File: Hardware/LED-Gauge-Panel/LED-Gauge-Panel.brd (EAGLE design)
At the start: 20.3 x 42.9 mm, 3 parts

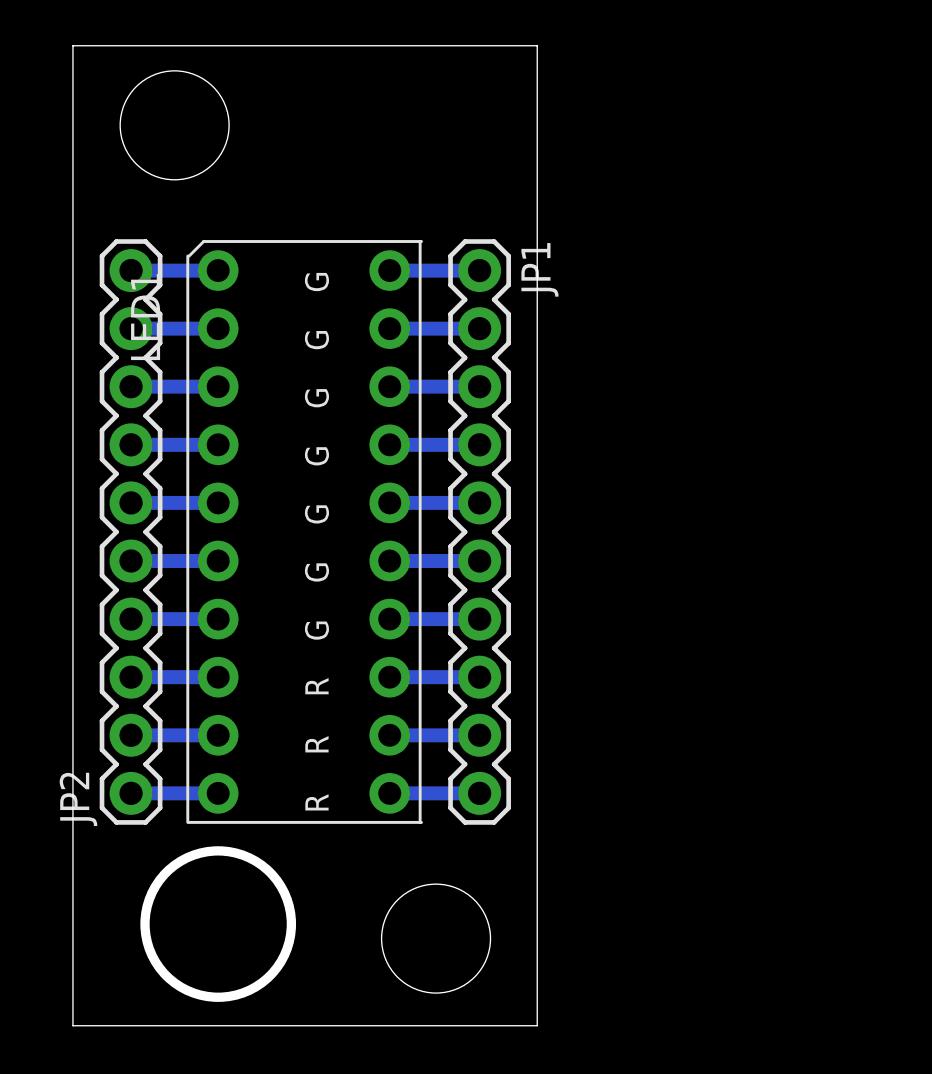
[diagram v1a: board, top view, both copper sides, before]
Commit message: Create library part for LED display button, update PCB with LED button part
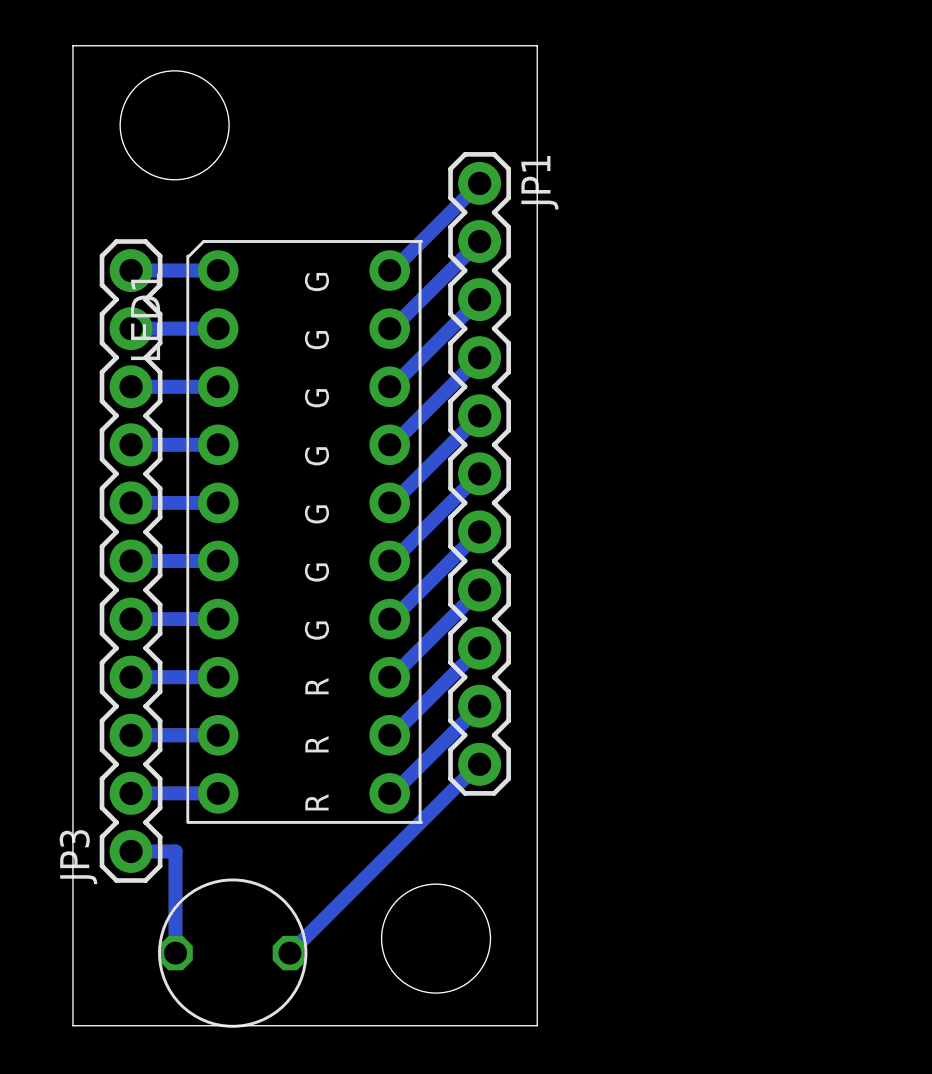
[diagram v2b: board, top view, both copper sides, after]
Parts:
- removed JP2: (no value), SparkFun-Connectors:1X10
- added JP3: (no value), SparkFun-Connectors:1X11
- added U$1: MOMENTARY-SWITCH-EVQ1, 2016PowerPackLibraries:EVQ11
- JP1: device SparkFun-Connectors:1X10 -> SparkFun-Connectors:1X11
- moved JP1 3.81 mm to (17.8, 36.8)
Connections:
- new net N$21: JP1.11, U$1.P$1
- new net N$22: JP3.1, U$1.P$2
- net N$11: now also JP3.11; no longer JP2.10
- net N$12: now also JP3.10; no longer JP2.9
- net N$13: now also JP3.9; no longer JP2.8
- net N$14: now also JP3.8; no longer JP2.7
- net N$15: now also JP3.7; no longer JP2.6
- net N$16: now also JP3.6; no longer JP2.5
- net N$17: now also JP3.5; no longer JP2.4
- net N$18: now also JP3.4; no longer JP2.3
- net N$19: now also JP3.3; no longer JP2.2
- net N$20: now also JP3.2; no longer JP2.1
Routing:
- net N$21: track 0.00 -> 11.7 mm
- net N$22: track 0.00 -> 6.39 mm
- net N$9: track 3.93 -> 5.51 mm
- net N$8: track 3.93 -> 5.51 mm
- net N$5: track 3.93 -> 5.51 mm
- net N$4: track 3.93 -> 5.51 mm
- net N$10: track 3.93 -> 5.51 mm
- net N$7: track 3.93 -> 5.51 mm
- net N$6: track 3.93 -> 5.51 mm
- net N$3: track 3.93 -> 5.51 mm
- net N$2: track 3.93 -> 5.51 mm
- net N$1: track 3.93 -> 5.51 mm
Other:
- outline, holes or cut-outs redrawn
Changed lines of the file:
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@@
 <hole x="15.875" y="3.81" drill="4.7625"/>
 <hole x="4.445" y="39.37" drill="4.7625"/>
-<circle x="6.35" y="4.445" radius="3.2" width="0.4064" layer="20"/>
 </plain>
 <attributes>
@@
 </autorouter>
 <elements>
-<element name="JP1" library="SparkFun-Connectors" package="1X10" value="" x="17.78" y="33.02" rot="R270">
-<attribute name="PROD_ID" value="CONN-11563" x="1.27" y="-5.08" size="1.778" layer="27" rot="R270" display="off"/>
-</element>
-<element name="JP2" library="SparkFun-Connectors" package="1X10" value="" x="2.54" y="10.16" rot="R90">
-<attribute name="PROD_ID" value="CONN-11563" x="24.13" y="48.26" size="1.778" layer="27" rot="R90" display="off"/>
-</element>
+<element name="JP1" library="SparkFun-Connectors" package="1X11" value="" x="17.78" y="36.83" rot="R270"/>
 <element name="LED1" library="2016PowerPackLibraries" package="LED-10" value="LED-DC7G3HWA" x="6.35" y="33.02" rot="R270"/>
+<element name="U$1" library="2016PowerPackLibraries" package="EVQ11" value="MOMENTARY-SWITCH-EVQ1" x="6.985" y="3.175" rot="R270"/>
+<element name="JP3" library="SparkFun-Connectors" package="1X11" value="" x="2.54" y="7.62" rot="R90"/>
 </elements>
 <signals>
@@
 <contactref element="LED1" pad="P$20"/>
 <contactref element="JP1" pad="1"/>
-<wire x1="13.85" y1="33.02" x2="17.78" y2="33.02" width="0.6096" layer="16"/>
+<wire x1="13.85" y1="33.02" x2="13.97" y2="33.02" width="0.6096" layer="16"/>
+<wire x1="13.97" y1="33.02" x2="17.78" y2="36.83" width="0.6096" layer="16"/>
 </signal>
 <signal name="N$2">
 <contactref element="LED1" pad="P$19"/>
 <contactref element="JP1" pad="2"/>
-<wire x1="13.85" y1="30.48" x2="17.78" y2="30.48" width="0.6096" layer="16"/>
+<wire x1="13.85" y1="30.48" x2="13.97" y2="30.48" width="0.6096" layer="16"/>
+<wire x1="13.97" y1="30.48" x2="17.78" y2="34.29" width="0.6096" layer="16"/>
 </signal>
 <signal name="N$3">
 <contactref element="LED1" pad="P$18"/>
 <contactref element="JP1" pad="3"/>
-<wire x1="13.85" y1="27.94" x2="17.78" y2="27.94" width="0.6096" layer="16"/>
+<wire x1="13.85" y1="27.94" x2="13.97" y2="27.94" width="0.6096" layer="16"/>
+<wire x1="13.97" y1="27.94" x2="17.78" y2="31.75" width="0.6096" layer="16"/>
 </signal>
 <signal name="N$4">
 <contactref element="LED1" pad="P$17"/>
 <contactref element="JP1" pad="4"/>
-<wire x1="13.85" y1="25.4" x2="17.78" y2="25.4" width="0.6096" layer="16"/>
+<wire x1="13.85" y1="25.4" x2="13.97" y2="25.4" width="0.6096" layer="16"/>
+<wire x1="13.97" y1="25.4" x2="17.78" y2="29.21" width="0.6096" layer="16"/>
 </signal>
 <signal name="N$5">
 <contactref element="LED1" pad="P$16"/>
 <contactref element="JP1" pad="5"/>
-<wire x1="13.85" y1="22.86" x2="17.78" y2="22.86" width="0.6096" layer="16"/>
+<wire x1="13.85" y1="22.86" x2="13.97" y2="22.86" width="0.6096" layer="16"/>
+<wire x1="13.97" y1="22.86" x2="17.78" y2="26.67" width="0.6096" layer="16"/>
 </signal>
 <signal name="N$6">
 <contactref element="LED1" pad="P$15"/>
 <contactref element="JP1" pad="6"/>
-<wire x1="13.85" y1="20.32" x2="17.78" y2="20.32" width="0.6096" layer="16"/>
+<wire x1="13.85" y1="20.32" x2="13.97" y2="20.32" width="0.6096" layer="16"/>
+<wire x1="13.97" y1="20.32" x2="17.78" y2="24.13" width="0.6096" layer="16"/>
 </signal>
 <signal name="N$7">
 <contactref element="LED1" pad="P$14"/>
 <contactref element="JP1" pad="7"/>
-<wire x1="13.85" y1="17.78" x2="17.78" y2="17.78" width="0.6096" layer="16"/>
+<wire x1="13.85" y1="17.78" x2="13.97" y2="17.78" width="0.6096" layer="16"/>
+<wire x1="13.97" y1="17.78" x2="17.78" y2="21.59" width="0.6096" layer="16"/>
 </signal>
 <signal name="N$8">
 <contactref element="LED1" pad="P$13"/>
 <contactref element="JP1" pad="8"/>
-<wire x1="13.85" y1="15.24" x2="17.78" y2="15.24" width="0.6096" layer="16"/>
+<wire x1="13.85" y1="15.24" x2="13.97" y2="15.24" width="0.6096" layer="16"/>
+<wire x1="13.97" y1="15.24" x2="17.78" y2="19.05" width="0.6096" layer="16"/>
 </signal>
 <signal name="N$9">
 <contactref element="LED1" pad="P$12"/>
 <contactref element="JP1" pad="9"/>
-<wire x1="13.85" y1="12.7" x2="17.78" y2="12.7" width="0.6096" layer="16"/>
+<wire x1="13.85" y1="12.7" x2="13.97" y2="12.7" width="0.6096" layer="16"/>
+<wire x1="13.97" y1="12.7" x2="17.78" y2="16.51" width="0.6096" layer="16"/>
 </signal>
 <signal name="N$10">
 <contactref element="JP1" pad="10"/>
 <contactref element="LED1" pad="P$11"/>
-<wire x1="13.85" y1="10.16" x2="17.78" y2="10.16" width="0.6096" layer="16"/>
+<wire x1="13.85" y1="10.16" x2="13.97" y2="10.16" width="0.6096" layer="16"/>
+<wire x1="13.97" y1="10.16" x2="17.78" y2="13.97" width="0.6096" layer="16"/>
 </signal>
 <signal name="N$11">
 <contactref element="LED1" pad="P$1"/>
-<contactref element="JP2" pad="10"/>
+<contactref element="JP3" pad="11"/>
 <wire x1="6.35" y1="33.02" x2="2.54" y2="33.02" width="0.6096" layer="16"/>
 </signal>
 <signal name="N$12">
-<contactref element="JP2" pad="9"/>
 <contactref element="LED1" pad="P$2"/>
+<contactref element="JP3" pad="10"/>
 <wire x1="6.35" y1="30.48" x2="2.54" y2="30.48" width="0.6096" layer="16"/>
 </signal>
 <signal name="N$13">
-<contactref element="JP2" pad="8"/>
 <contactref element="LED1" pad="P$3"/>
+<contactref element="JP3" pad="9"/>
 <wire x1="6.35" y1="27.94" x2="2.54" y2="27.94" width="0.6096" layer="16"/>
 </signal>
 <signal name="N$14">
-<contactref element="JP2" pad="7"/>
 <contactref element="LED1" pad="P$4"/>
+<contactref element="JP3" pad="8"/>
 <wire x1="6.35" y1="25.4" x2="2.54" y2="25.4" width="0.6096" layer="16"/>
 </signal>
 <signal name="N$15">
-<contactref element="JP2" pad="6"/>
 <contactref element="LED1" pad="P$5"/>
-<wire x1="6.35" y1="22.86" x2="2.54" y2="22.86" width="0.6096" layer="16"/>
+<contactref element="JP3" pad="7"/>
+<wire x1="2.54" y1="22.86" x2="6.35" y2="22.86" width="0.6096" layer="16"/>
 </signal>
 <signal name="N$16">
-<contactref element="JP2" pad="5"/>
 <contactref element="LED1" pad="P$6"/>
-<wire x1="6.35" y1="20.32" x2="2.54" y2="20.32" width="0.6096" layer="16"/>
+<contactref element="JP3" pad="6"/>
+<wire x1="2.54" y1="20.32" x2="6.35" y2="20.32" width="0.6096" layer="16"/>
 </signal>
 <signal name="N$17">
-<contactref element="JP2" pad="4"/>
 <contactref element="LED1" pad="P$7"/>
-<wire x1="6.35" y1="17.78" x2="2.54" y2="17.78" width="0.6096" layer="16"/>
+<contactref element="JP3" pad="5"/>
+<wire x1="2.54" y1="17.78" x2="6.35" y2="17.78" width="0.6096" layer="16"/>
 </signal>
 <signal name="N$18">
-<contactref element="JP2" pad="3"/>
 <contactref element="LED1" pad="P$8"/>
-<wire x1="6.35" y1="15.24" x2="2.54" y2="15.24" width="0.6096" layer="16"/>
+<contactref element="JP3" pad="4"/>
+<wire x1="2.54" y1="15.24" x2="6.35" y2="15.24" width="0.6096" layer="16"/>
 </signal>
 <signal name="N$19">
-<contactref element="JP2" pad="2"/>
 <contactref element="LED1" pad="P$9"/>
-<wire x1="6.35" y1="12.7" x2="2.54" y2="12.7" width="0.6096" layer="16"/>
+<contactref element="JP3" pad="3"/>
+<wire x1="2.54" y1="12.7" x2="6.35" y2="12.7" width="0.6096" layer="16"/>
 </signal>
 <signal name="N$20">
-<contactref element="JP2" pad="1"/>
 <contactref element="LED1" pad="P$10"/>
-<wire x1="6.35" y1="10.16" x2="2.54" y2="10.16" width="0.6096" layer="16"/>
+<contactref element="JP3" pad="2"/>
+<wire x1="2.54" y1="10.16" x2="6.35" y2="10.16" width="0.6096" layer="16"/>
+</signal>
+<signal name="N$21">
+<contactref element="JP1" pad="11"/>
+<contactref element="U$1" pad="P$1"/>
+<wire x1="17.78" y1="11.43" x2="17.74" y2="11.43" width="0.6096" layer="16"/>
+<wire x1="17.74" y1="11.43" x2="9.485" y2="3.175" width="0.6096" layer="16"/>
+</signal>
+<signal name="N$22">
+<contactref element="U$1" pad="P$2"/>
+<contactref element="JP3" pad="1"/>
+<wire x1="2.54" y1="7.62" x2="4.485" y2="7.62" width="0.6096" layer="16"/>
+<wire x1="4.485" y1="7.62" x2="4.485" y2="3.175" width="0.6096" layer="16"/>
 </signal>
 </signals>
